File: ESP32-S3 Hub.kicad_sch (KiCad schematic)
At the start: 23 parts, among them U1 ESP32-S3, Y1 ABM11-40.000MHZ-B1U-T3, 10ppm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

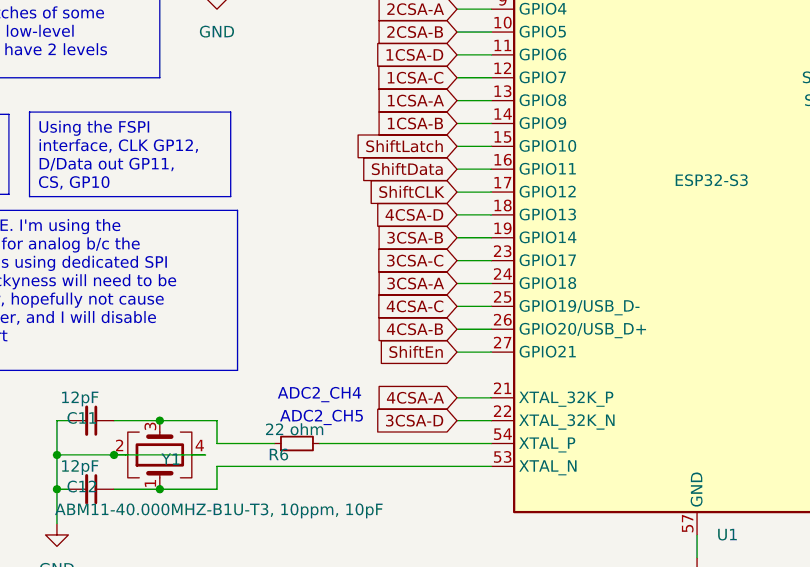
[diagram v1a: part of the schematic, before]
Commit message: Corrected footprint, started reconnect nets PCB
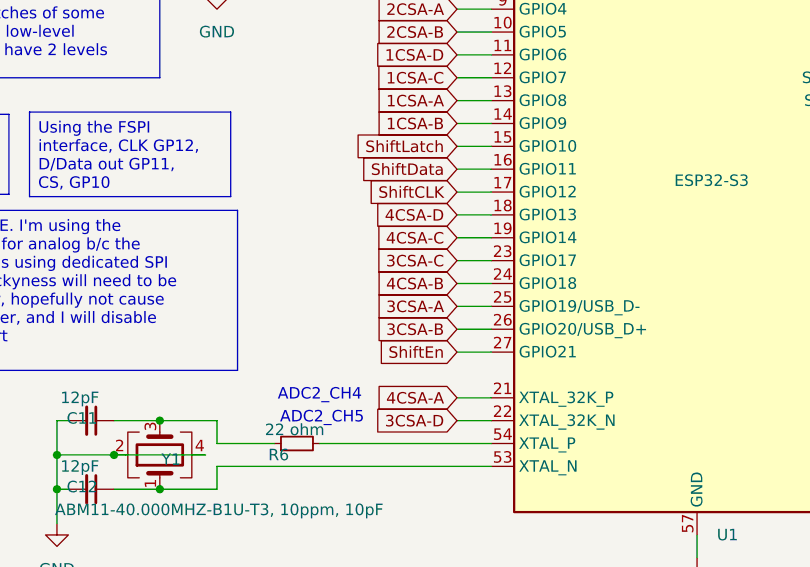
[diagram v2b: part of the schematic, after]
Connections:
- net 3CSA-A: now also U1.25 (GPIO19/USB_D-); no longer U1.24 (GPIO18)
- net 3CSA-B: now also U1.26 (GPIO20/USB_D+); no longer U1.19 (GPIO14)
- net 4CSA-B: now also U1.24 (GPIO18); no longer U1.26 (GPIO20/USB_D+)
- net 4CSA-C: now also U1.19 (GPIO14); no longer U1.25 (GPIO19/USB_D-)

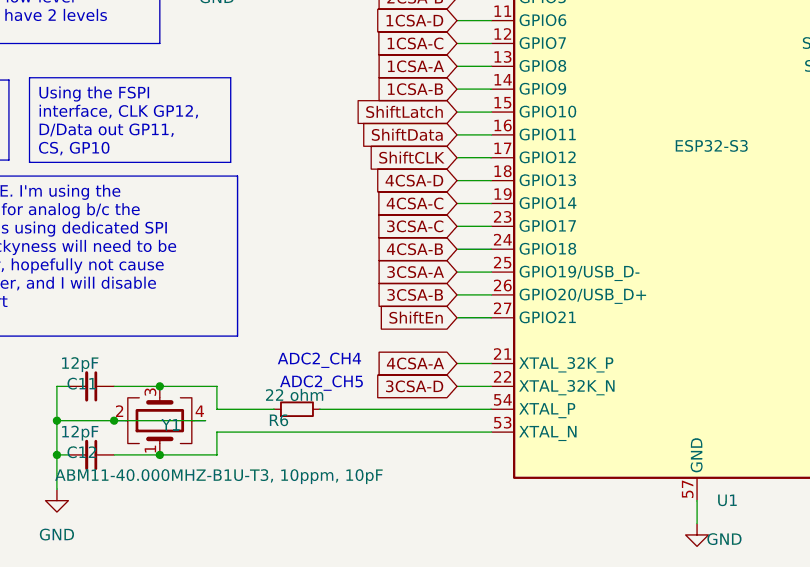
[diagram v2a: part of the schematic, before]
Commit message: Finished Reroute of ESP32-s3 hub
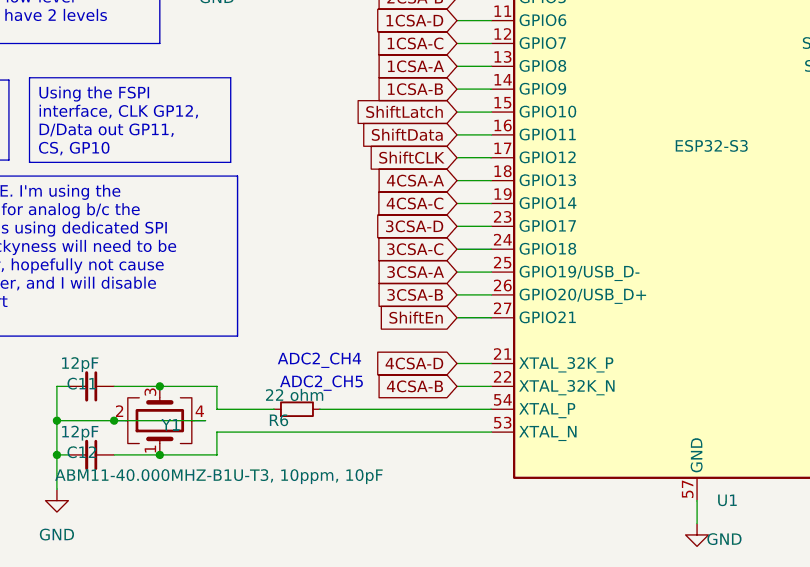
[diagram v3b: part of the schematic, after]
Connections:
- net 3CSA-C: now also U1.24 (GPIO18); no longer U1.23 (GPIO17)
- net 3CSA-D: now also U1.23 (GPIO17); no longer U1.22 (XTAL_32K_N)
- net 4CSA-A: now also U1.18 (GPIO13); no longer U1.21 (XTAL_32K_P)
- net 4CSA-B: now also U1.22 (XTAL_32K_N); no longer U1.24 (GPIO18)
- net 4CSA-D: now also U1.21 (XTAL_32K_P); no longer U1.18 (GPIO13)

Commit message: Improve schematic consistency
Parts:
- U1: value ESP32-S3 -> ESP32-S3 FN8
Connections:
- net 1CSA-A renamed ADC-1A
- net 1CSA-B renamed ADC-1B
- net 1CSA-C renamed ADC-1C
- net 1CSA-D renamed ADC-1D
- net 2CSA-A renamed ADC-2A
- net 2CSA-B renamed ADC-2B
- net 2CSA-C renamed ADC-2C
- net 2CSA-D renamed ADC-2D
- net 3CSA-A renamed ADC-3A
- net 3CSA-B renamed ADC-3B
- net 3CSA-C renamed ADC-3C
- net 3CSA-D renamed ADC-3D
- net 4CSA-A renamed ADC-4A
- net 4CSA-B renamed ADC-4B
- net 4CSA-C renamed ADC-4C
- net 4CSA-D renamed ADC-4D
- net CS1 renamed CS-1
- net CS2 renamed CS-2
- net CS3 renamed CS-3
- net CS4 renamed CS-4
- net Free1 renamed Free-1
- net Free2 renamed Free-2
- net MISO1 renamed MISO
- net MOSI1 renamed MOSI
- net SCK1 renamed SCK
- net SCL1 renamed SCL
- net SDA1 renamed SDA
- net UART0-RTS/CS0 renamed UART0-RTS
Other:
- note removed: "When IO1 is high & combined w/ GPIO 46 high, will enter a special SPI boot mode"
- moved on the sheet: R8, R9

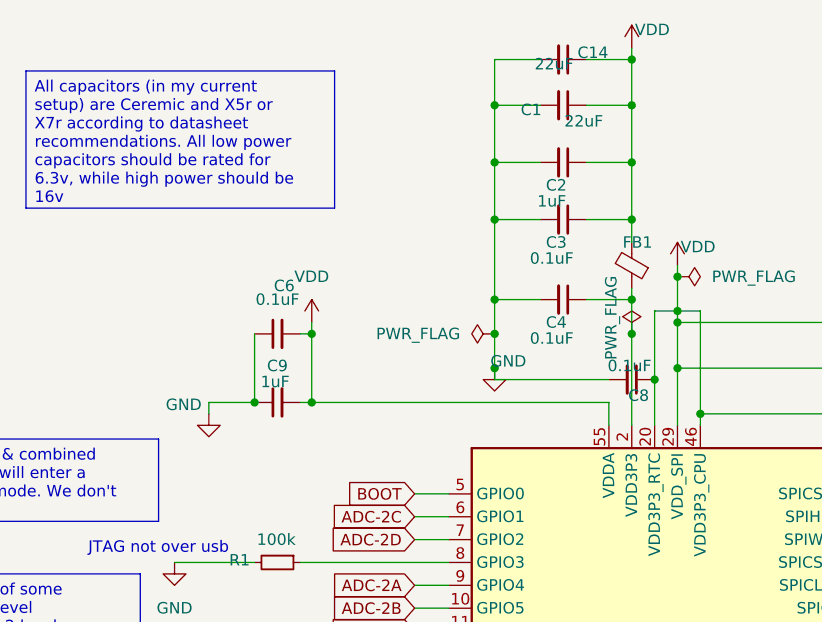
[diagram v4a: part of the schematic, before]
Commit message: Removed unnecessary ferrite bead
There is no radio on this design to worry about power coupling
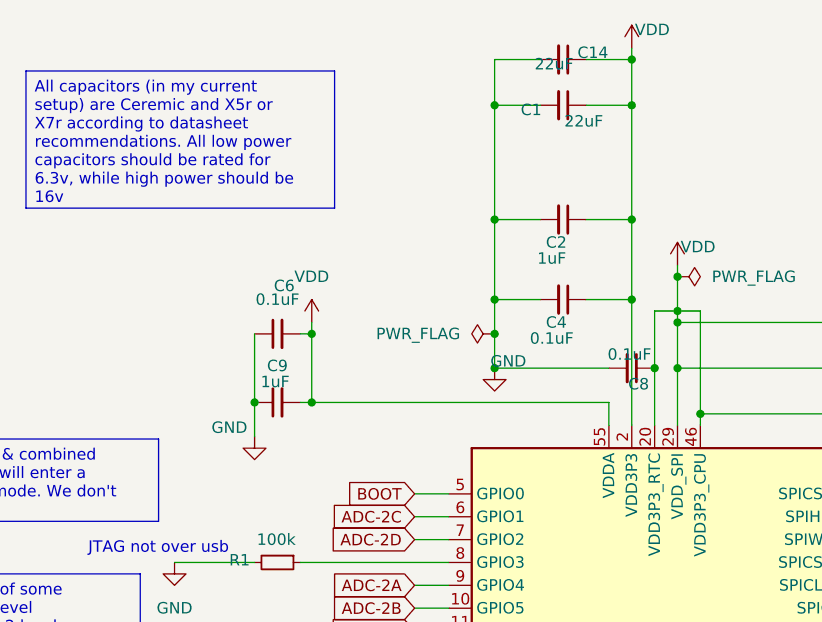
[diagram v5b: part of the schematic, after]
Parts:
- removed C3: 0.1uF, Capacitor_SMD:C_0402_1005Metric, symbol Device:C_Small
- removed FB1: 120ohm imp @100mhz, 1 amp, Inductor_SMD:L_0402_1005Metric, symbol Device:FerriteBead_Small
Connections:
- net VDD: now also C4.1, U1.2 (VDD3P3), U1.3 (VDD3P3)
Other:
- moved on the sheet: C2, C8

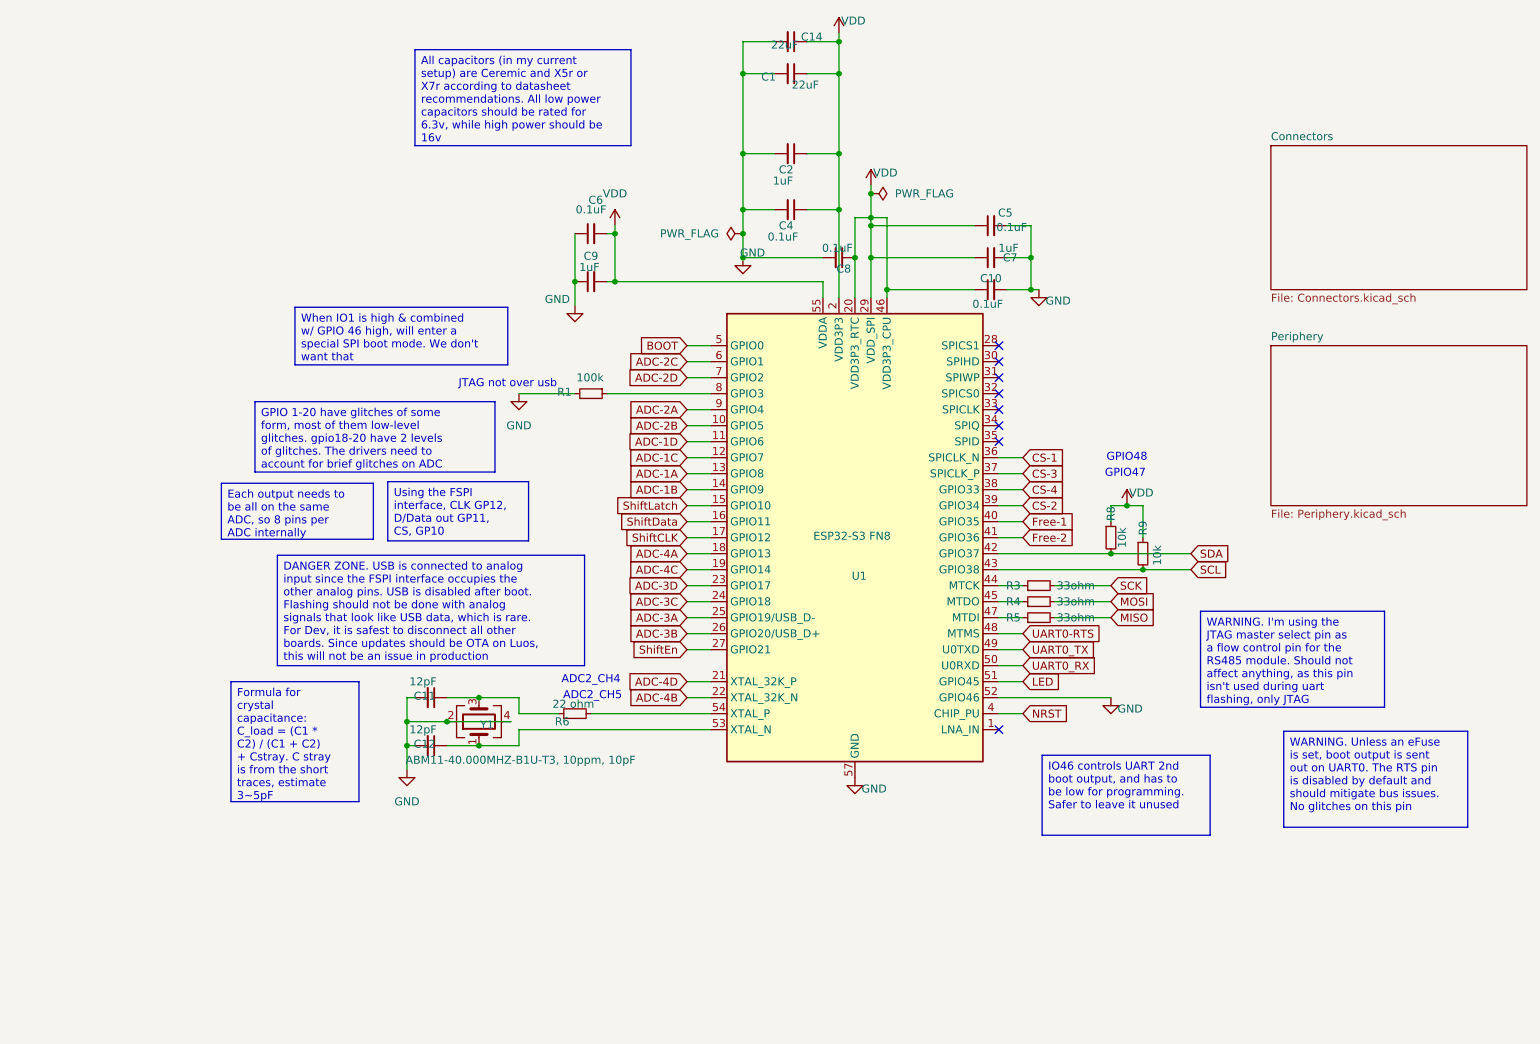
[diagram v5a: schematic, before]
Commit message: Clarified capacitors for main chip
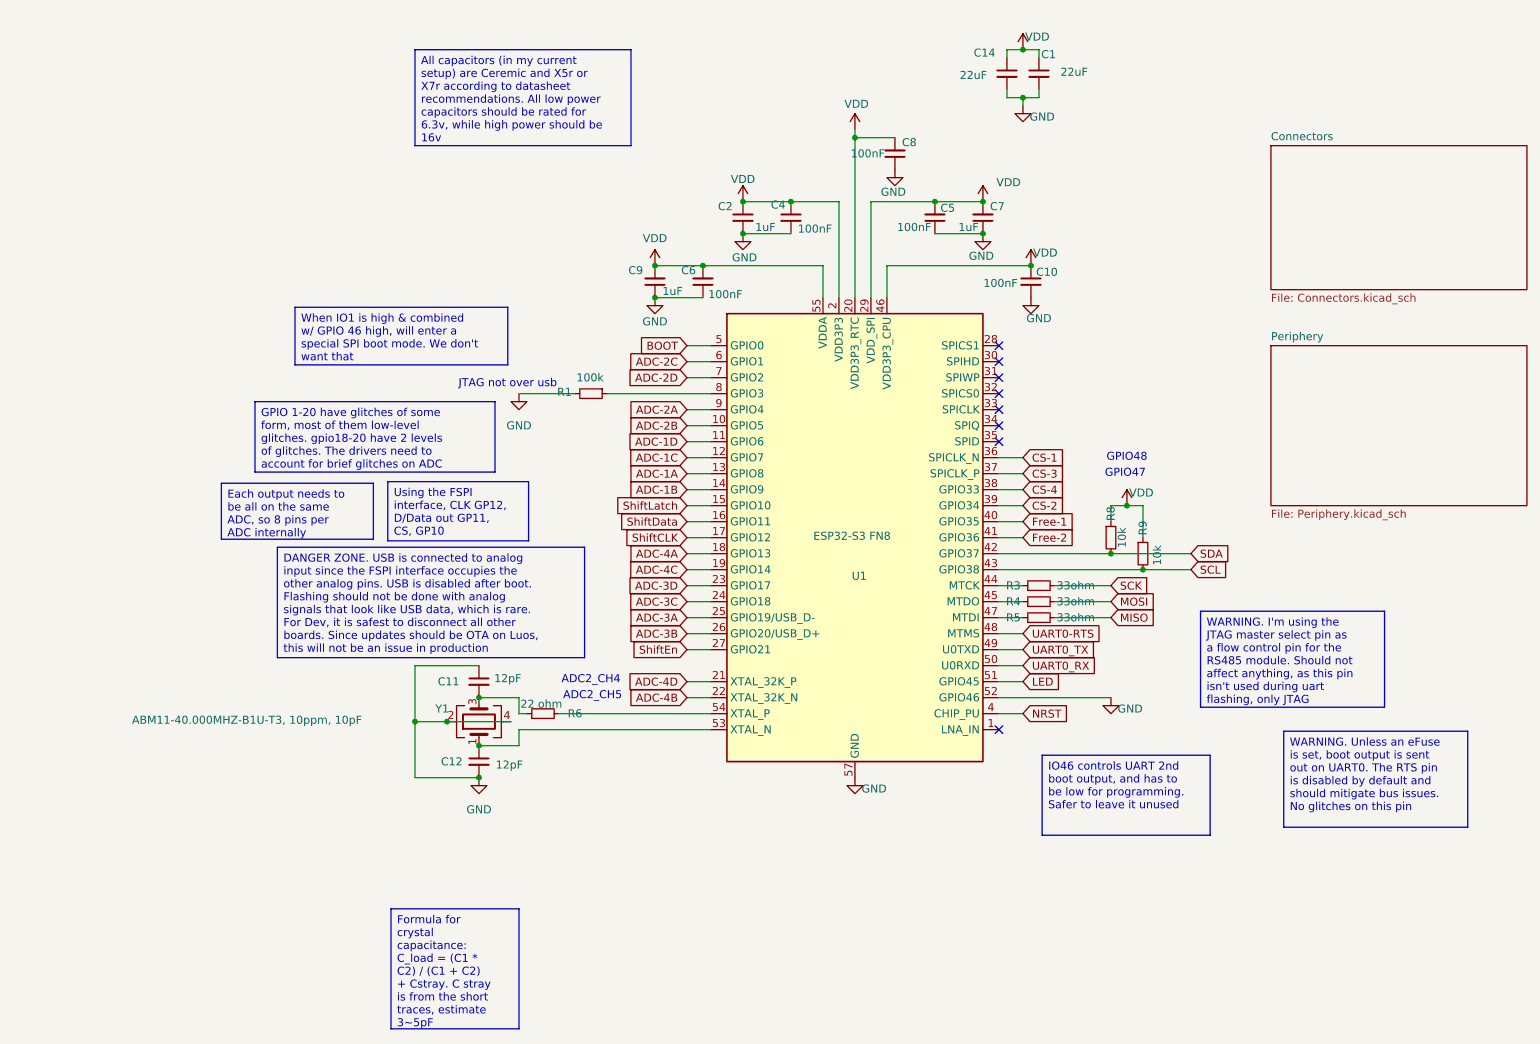
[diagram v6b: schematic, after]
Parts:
- C10, C4, C5, C6, C8: value 0.1uF -> 100nF
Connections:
- net GND: now also C11.1, C5.1, C7.1, C8.1; no longer C11.2, C5.2, C7.2, C8.2
- net VDD: now also C5.2, C7.2, C8.2; no longer C5.1, C7.1, C8.1
- net at R6.1, Y1.3: now also C11.2; no longer C11.1
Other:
- moved on the sheet: C1, C10, C11, C12, C14, C2, C4, C5, C6, C7, C8, C9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

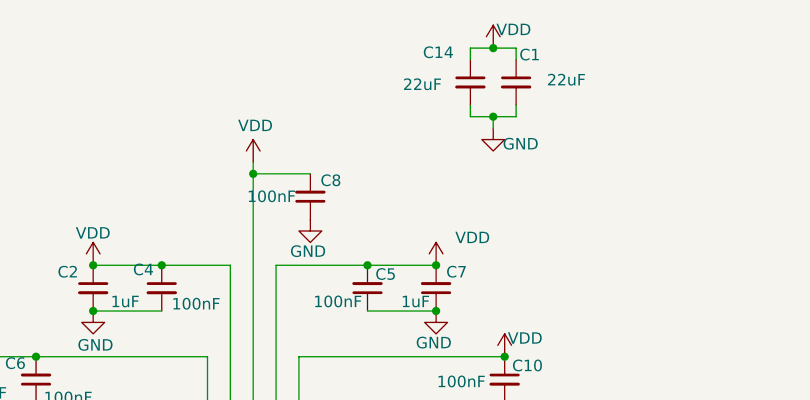
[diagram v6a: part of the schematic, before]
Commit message: Fixed ERC power flag issues
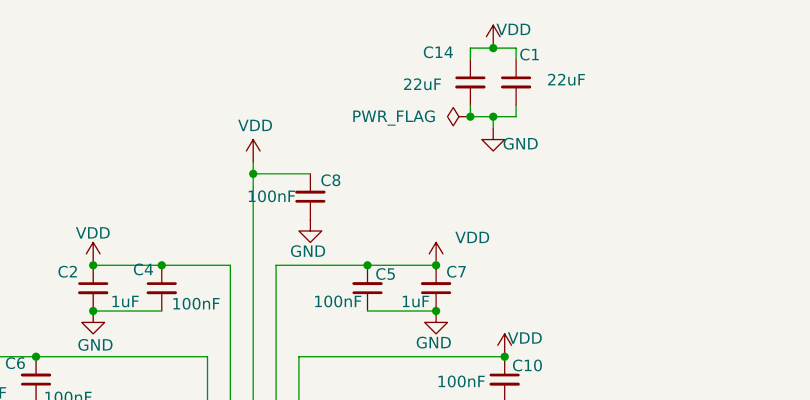
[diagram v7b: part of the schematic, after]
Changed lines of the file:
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@@
+	)
+	(junction
+		(at 168.91 22.86)
+		(diameter 0)
+		(color 0 0 0 0)
 	)
 	(junction
@@
 					(unit 1)
 				)
+			)
+		)
+	)
+	(symbol
+		(lib_id "power:PWR_FLAG")
+		(at 168.91 22.86 90)
+		(unit 1)
+		(exclude_from_sim no)
+		(in_bom yes)
+		(on_board yes)
+		(dnp no)
+		(fields_autoplaced yes)
+		(property "Reference" "#FLG01"
+			(at 167.005 22.86 0)
+			(effects
+				(font
+					(size 1.27 1.27)
+				)
+				(hide yes)
+			)
+		)
+		(property "Value" "PWR_FLAG"
+			(at 165.1 22.8599 90)
+			(effects
+				(font
+					(size 1.27 1.27)
+				)
+				(justify left)
+			)
+		)
+		(property "Footprint" ""
+			(at 168.91 22.86 0)
+			(effects
+				(font
+					(size 1.27 1.27)
+				)
+				(hide yes)
+			)
+		)
+		(property "Datasheet" "~"
+			(at 168.91 22.86 0)
+			(effects
+				(font
+					(size 1.27 1.27)
+				)
+				(hide yes)
+			)
+		)
+		(property "Description" "Special symbol for telling ERC where power comes from"
+			(at 168.91 22.86 0)
+			(effects
+				(font
+					(size 1.27 1.27)
+				)
+				(hide yes)
+			)
+		)
+		(pin "1"
+		)
+		(instances
+			(project ""
+				(path "/a8c80fba-3bca-4358-b5bb-9ebf9383c658"
+					(reference "#FLG01")
+					(unit 1)
+				)
